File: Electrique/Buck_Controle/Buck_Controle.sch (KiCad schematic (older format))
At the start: 0 parts

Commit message: footprint - pcb build
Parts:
- added Cboot1: 10nF, Capacitor_SMD:C_0805_2012Metric, symbol Device:C_Small
- added Cin1, Cin2, Cin3: 10uF, Capacitor_SMD:C_0805_2012Metric, symbol Device:C_Small
- added Cout1: 330uF, Buck_Controle:CAP_TANT_2917, symbol Device:CP1_Small
- added D1: SBRD10200TR, Diode_SMD:D_SMC, symbol Device:D
- added L1: 15uH, Inductor_SMD:L_Bourns_SRR1210A, symbol Device:L
- added Rfbb1: 3.24k, Resistor_SMD:R_0805_2012Metric, symbol Device:R
- added Rfbt1: 10k, Resistor_SMD:R_0805_2012Metric, symbol Device:R
- added U1: TPS5450DDA, Package_SO:TI_SO-PowerPAD-8_ThermalVias, symbol Custom_parts:TPS5450DDA
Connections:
- new net: Cboot1.1, D1.1 (K), L1.2, U1.1 (BOOT)
- new net: Rfbb1.1, Rfbt1.2, U1.4 (VSENSE)
- new net: Cboot1.2, U1.8 (PH)
- new net +BATT: Cin1.1, Cin2.1, Cin3.1, U1.7 (VIN)
- new net GND: Cin1.2, Cin2.2, Cin3.2, Cout1.2, D1.2 (A), Rfbb1.2, U1.6 (GND), U1.9 (PW_PAD)
- new net Vout: Cout1.1, L1.1, Rfbt1.1
- no-connect marks 0 -> 1

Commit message: Continuation PCB controle
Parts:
- added J?: Conn_01x02_Female, symbol Connector:Conn_01x02_Female
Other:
- moved on the sheet: Cboot1, Cin1, Cin2, Cin3, Cout1, D1, L1, Rfbb1, Rfbt1, U1

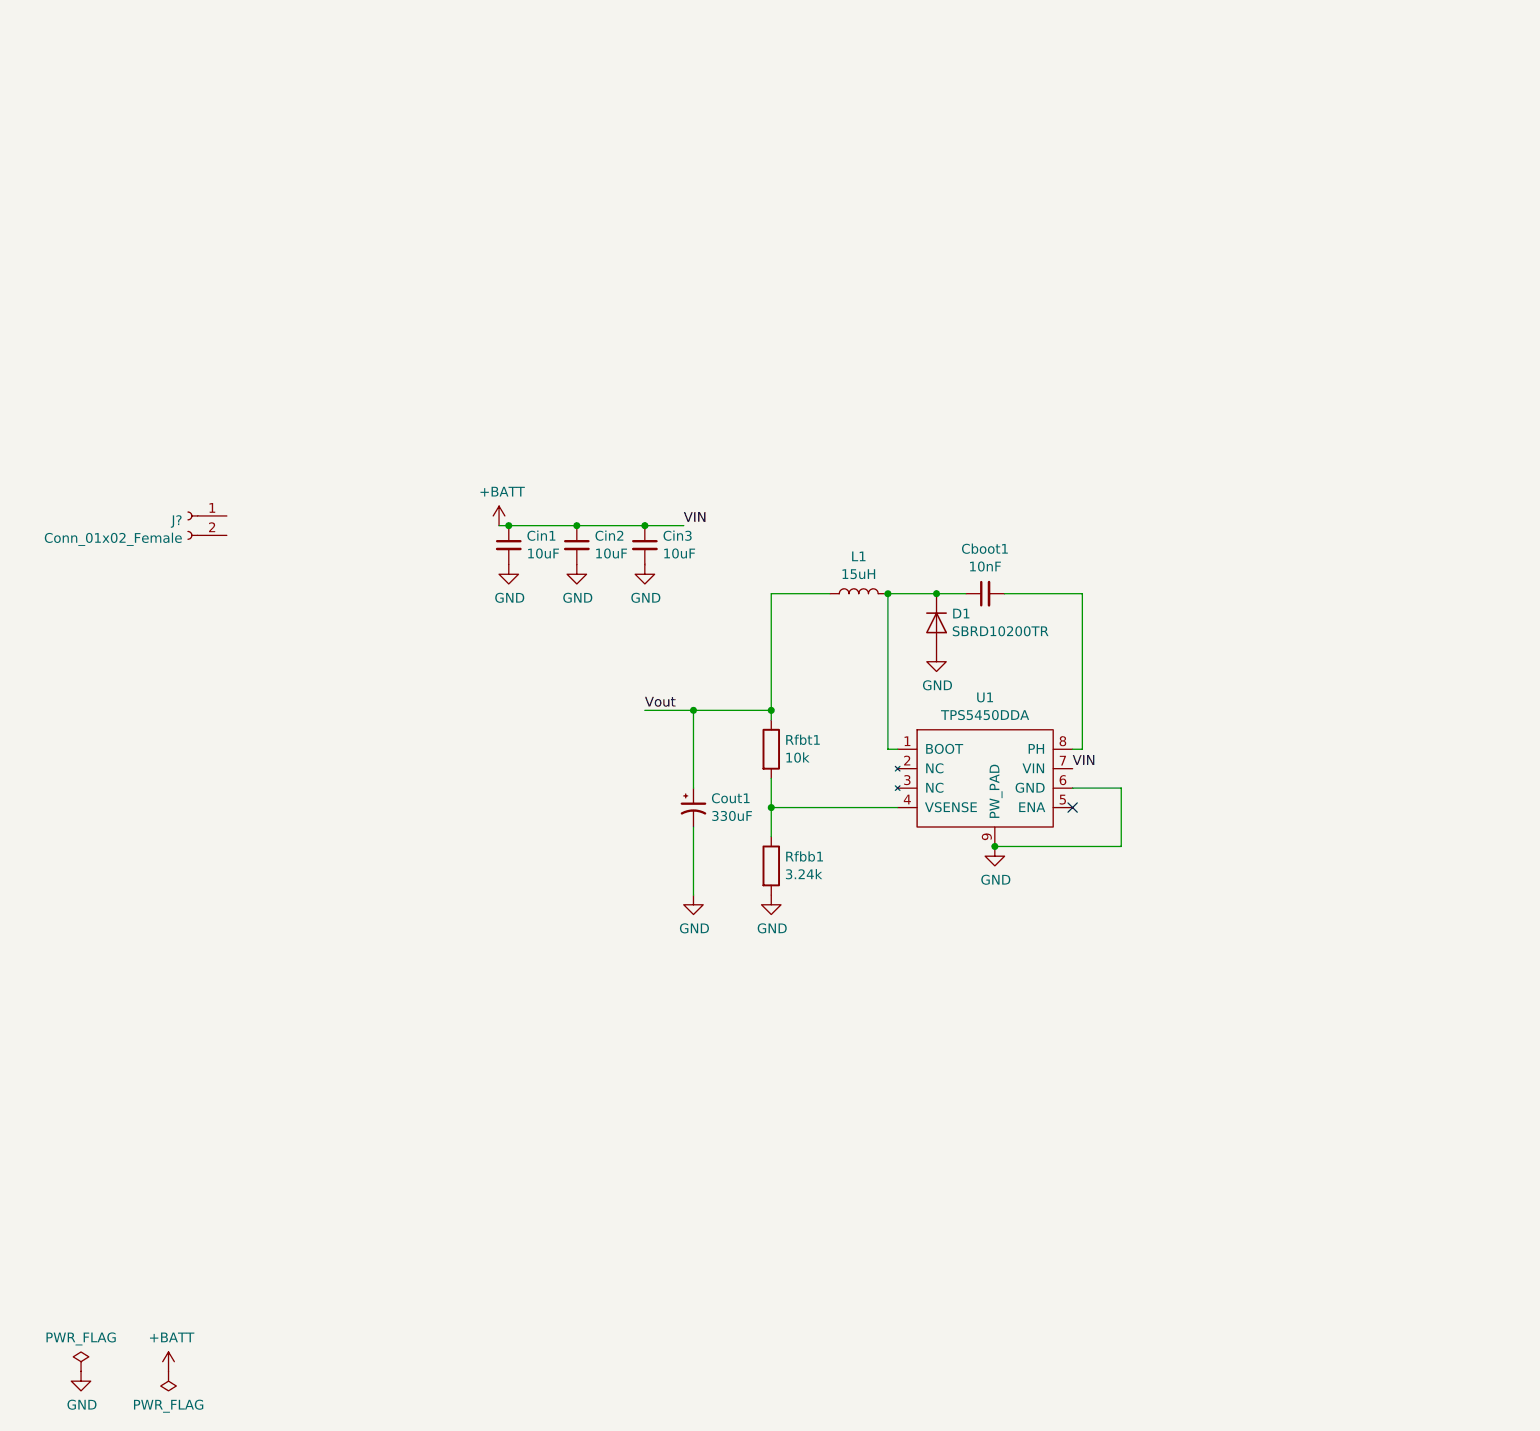
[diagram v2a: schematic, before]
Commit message: Ajout pieces manquantes Boost
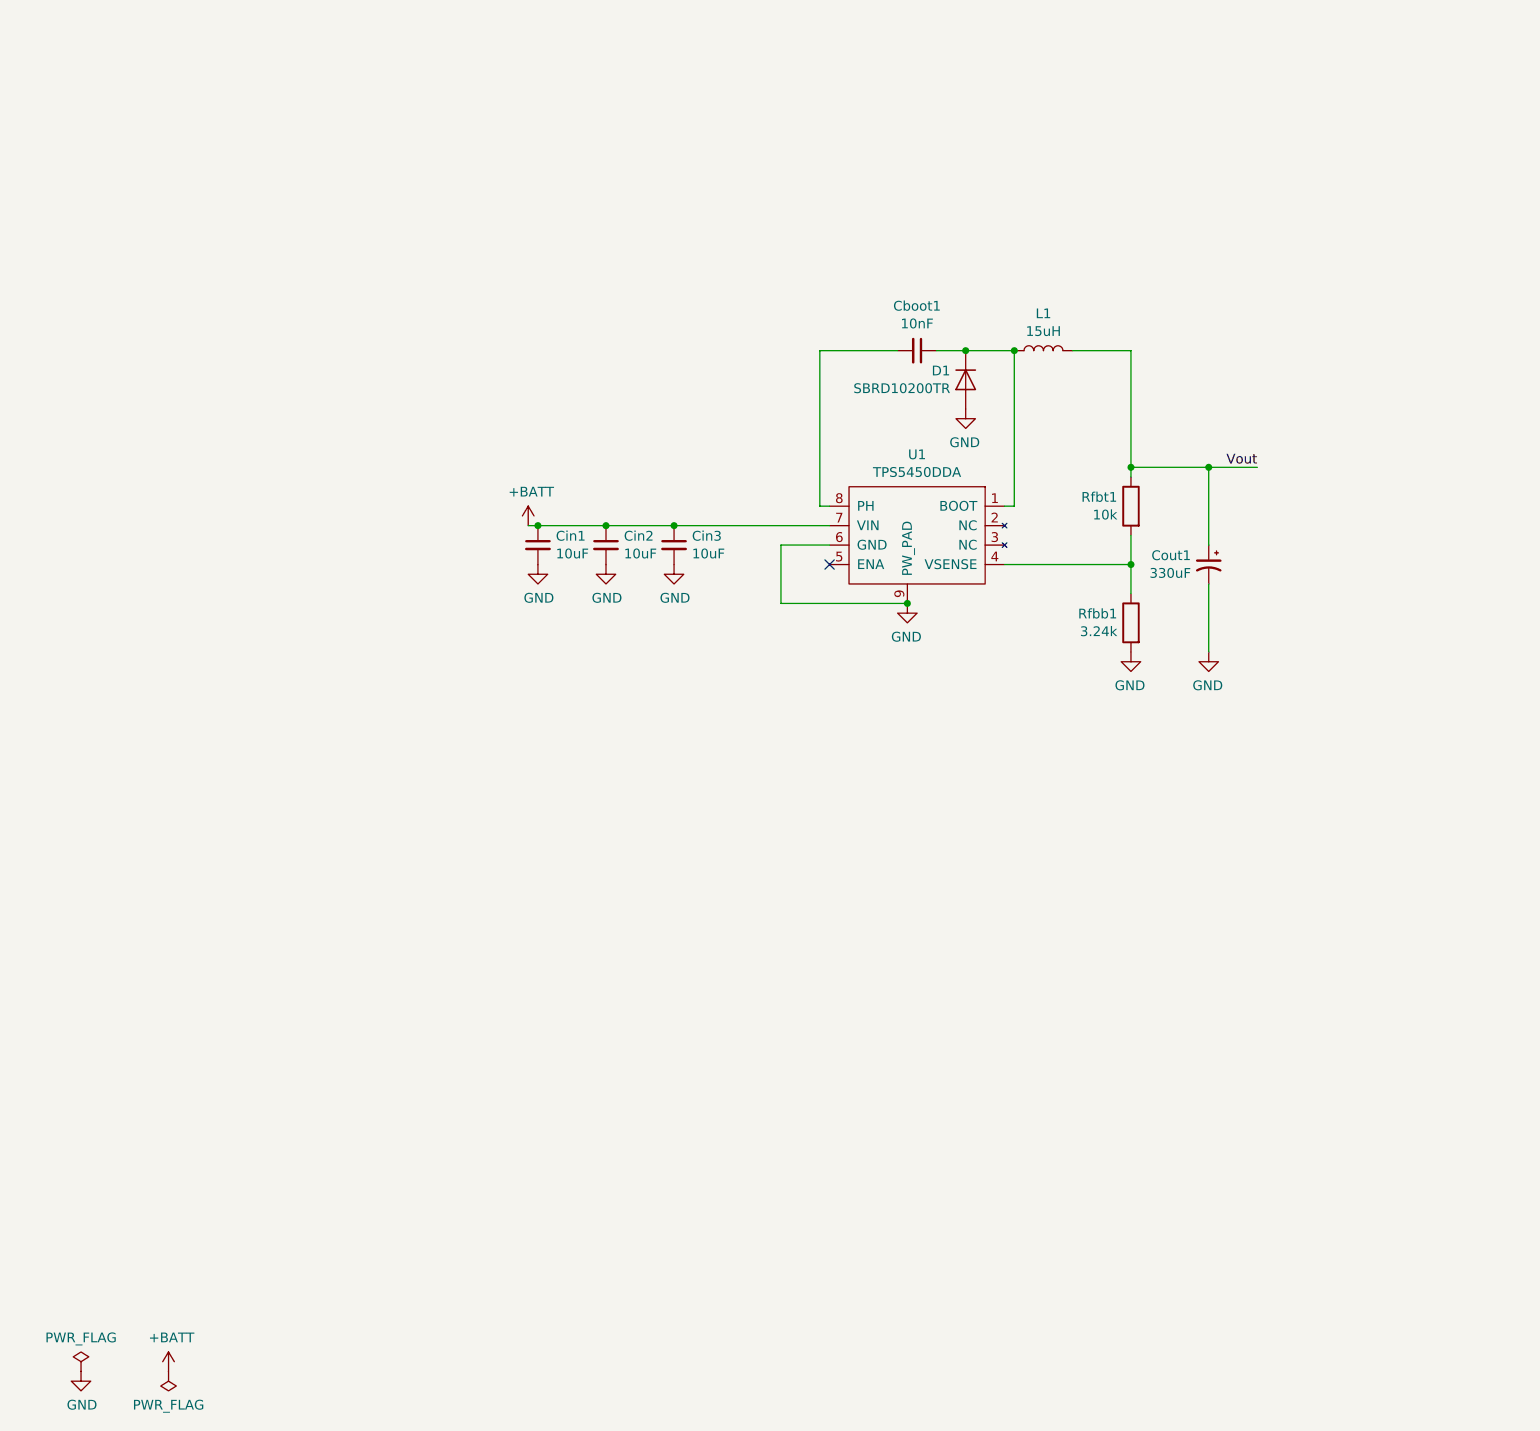
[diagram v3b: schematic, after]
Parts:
- removed J?: Conn_01x02_Female, symbol Connector:Conn_01x02_Female
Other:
- moved on the sheet: Cboot1, Cin1, Cin2, Cin3, Cout1, D1, L1, Rfbb1, Rfbt1, U1

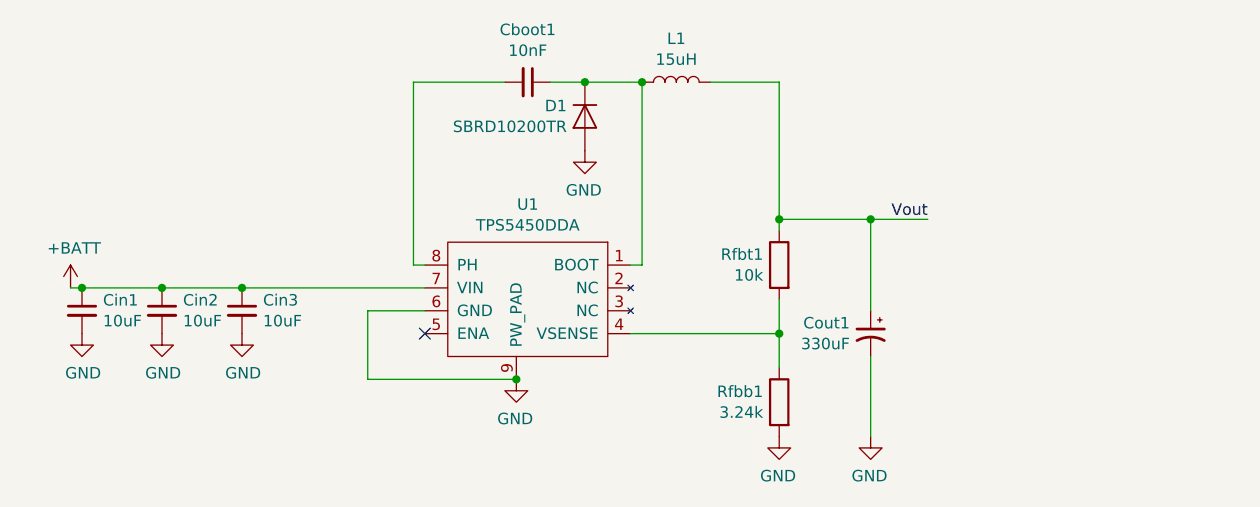
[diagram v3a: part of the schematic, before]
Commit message: Ajout du bus in/out
Ajout du bus pour in/out + routage sur la couche du dessous + via pour transférer ces signaux sur les 2 couches
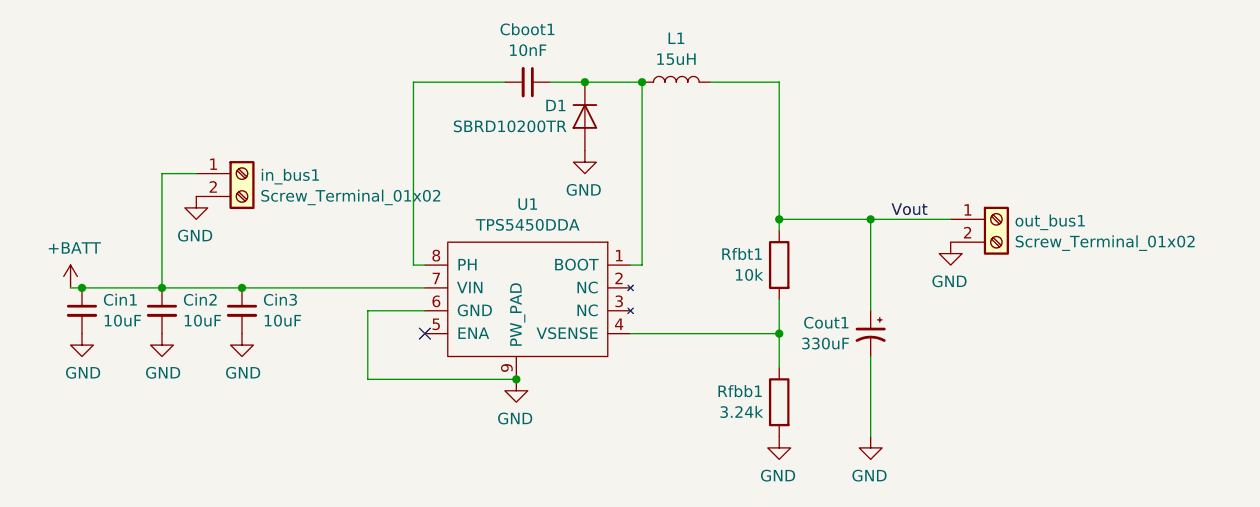
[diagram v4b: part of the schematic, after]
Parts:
- added in_bus1, out_bus1: Screw_Terminal_01x02, TerminalBlock:TerminalBlock_bornier-2_P5.08mm, symbol Connector:Screw_Terminal_01x02
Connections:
- net +BATT: now also in_bus1.1 (Pin_1)
- net GND: now also in_bus1.2 (Pin_2), out_bus1.2 (Pin_2)
- net Vout: now also out_bus1.1 (Pin_1)
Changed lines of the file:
@@
 Wire Wire Line
 	7100 3600 7100 3950
-Wire Wire Line
-	7100 3000 7350 3000
 Connection ~ 7100 3000
 Text Label 7350 3000 2    50   ~ 0
@@
 Wire Wire Line
 	4350 3300 5150 3300
+$Comp
+L Connector:Screw_Terminal_01x02 in_bus1
+U 1 1 5FBC6AC6
+P 4350 2800
+F 0 "in_bus1" H 4430 2792 50  0000 L CNN
+F 1 "Screw_Terminal_01x02" H 4430 2701 50  0000 L CNN
+F 2 "TerminalBlock:TerminalBlock_bornier-2_P5.08mm" H 4350 2800 50  0001 C CNN
+F 3 "~" H 4350 2800 50  0001 C CNN
+	1    4350 2800
+	1    0    0    -1
+$EndComp
+$Comp
+L Connector:Screw_Terminal_01x02 out_bus1
+U 1 1 5FBC7ECB
+P 7650 3000
+F 0 "out_bus1" H 7730 2992 50  0000 L CNN
+F 1 "Screw_Terminal_01x02" H 7730 2901 50  0000 L CNN
+F 2 "TerminalBlock:TerminalBlock_bornier-2_P5.08mm" H 7650 3000 50  0001 C CNN
+F 3 "~" H 7650 3000 50  0001 C CNN
+	1    7650 3000
+	1    0    0    -1
+$EndComp
+$Comp
+L power:GND #PWR0111
+U 1 1 5FBC9301
+P 7450 3100
+F 0 "#PWR0111" H 7450 2850 50  0001 C CNN
+F 1 "GND" H 7455 2927 50  0000 C CNN
+F 2 "" H 7450 3100 50  0001 C CNN
+F 3 "" H 7450 3100 50  0001 C CNN
+	1    7450 3100
+	-1   0    0    -1
+$EndComp
+$Comp
+L power:GND #PWR0112
+U 1 1 5FBCA470
+P 4150 2900
+F 0 "#PWR0112" H 4150 2650 50  0001 C CNN
+F 1 "GND" H 4155 2727 50  0000 C CNN
+F 2 "" H 4150 2900 50  0001 C CNN
+F 3 "" H 4150 2900 50  0001 C CNN
+	1    4150 2900
+	-1   0    0    -1
+$EndComp
+Wire Wire Line
+	4150 2800 4000 2800
+Wire Wire Line
+	4000 2800 4000 3300
+Wire Wire Line
+	7100 3000 7450 3000
 $EndSCHEMATC

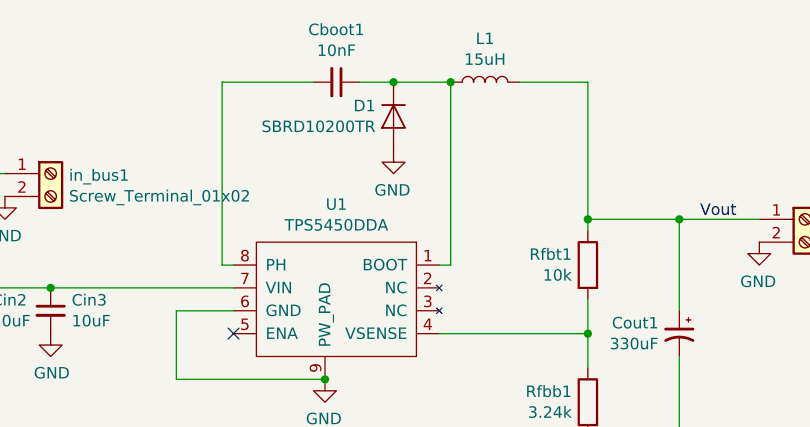
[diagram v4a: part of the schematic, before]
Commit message: Changement du branchement de Cboot + DRC pcb controle
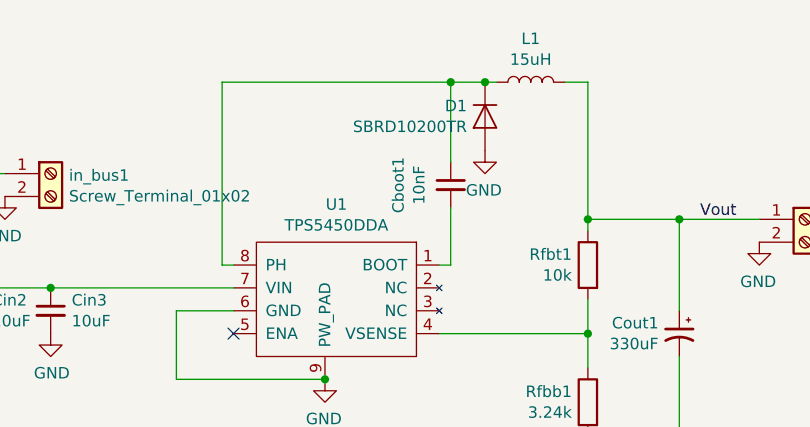
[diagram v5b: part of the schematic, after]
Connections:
- net at Cboot1.1, D1.1 (K), L1.2: now also U1.8 (PH); no longer U1.1 (BOOT)
- net at Cboot1.2: now also U1.1 (BOOT); no longer U1.8 (PH)
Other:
- moved on the sheet: Cboot1, D1, L1
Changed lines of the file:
@@
 L Device:C_Small Cboot1
 U 1 1 5E446D6F
-P 5600 2400
-F 0 "Cboot1" V 5829 2400 50  0000 C CNN
-F 1 "10nF" V 5738 2400 50  0000 C CNN
-F 2 "Capacitor_SMD:C_0805_2012Metric" H 5600 2400 50  0001 C CNN
-F 3 "~" H 5600 2400 50  0001 C CNN
-	1    5600 2400
-	0    1    -1   0
+P 6100 2850
+F 0 "Cboot1" V 6329 2850 50  0000 C CNN
+F 1 "10nF" V 6238 2850 50  0000 C CNN
+F 2 "Capacitor_SMD:C_0805_2012Metric" H 6100 2850 50  0001 C CNN
+F 3 "~" H 6100 2850 50  0001 C CNN
+	1    6100 2850
+	-1   0    0    -1
 $EndComp
 Wire Wire Line
 	6100 3200 6050 3200
 Wire Wire Line
-	5500 2400 5100 2400
-Wire Wire Line
 	5100 3200 5150 3200
 Wire Wire Line
-	5700 2400 5850 2400
-Wire Wire Line
 	5100 2400 5100 3200
 Wire Wire Line
-	6100 2400 6100 3200
+	6100 2400 6100 2750
 $Comp
 L Device:D D1
 U 1 1 5E44E25D
-P 5850 2550
-F 0 "D1" V 5804 2629 50  0000 L CNN
-F 1 "SBRD10200TR" V 5895 2629 50  0000 L CNN
-F 2 "Diode_SMD:D_SMC" H 5850 2550 50  0001 C CNN
-F 3 "~" H 5850 2550 50  0001 C CNN
-	1    5850 2550
+P 6250 2550
+F 0 "D1" V 6204 2629 50  0000 L CNN
+F 1 "SBRD10200TR" V 6295 2629 50  0000 L CNN
+F 2 "Diode_SMD:D_SMC" H 6250 2550 50  0001 C CNN
+F 3 "~" H 6250 2550 50  0001 C CNN
+	1    6250 2550
 	0    -1   1    0
 $EndComp
-Connection ~ 5850 2400
-Wire Wire Line
-	5850 2400 6100 2400
 $Comp
 L power:GND #PWR0104
 U 1 1 5E44E60C
-P 5850 2700
-F 0 "#PWR0104" H 5850 2450 50  0001 C CNN
-F 1 "GND" H 5855 2527 50  0000 C CNN
-F 2 "" H 5850 2700 50  0001 C CNN
-F 3 "" H 5850 2700 50  0001 C CNN
-	1    5850 2700
+P 6250 2700
+F 0 "#PWR0104" H 6250 2450 50  0001 C CNN
+F 1 "GND" H 6255 2527 50  0000 C CNN
+F 2 "" H 6250 2700 50  0001 C CNN
+F 3 "" H 6250 2700 50  0001 C CNN
+	1    6250 2700
 	-1   0    0    -1
 $EndComp
@@
 L Device:L L1
 U 1 1 5E44F76F
-P 6250 2400
-F 0 "L1" V 6440 2400 50  0000 C CNN
-F 1 "15uH" V 6349 2400 50  0000 C CNN
-F 2 "Inductor_SMD:L_Bourns_SRR1210A" H 6250 2400 50  0001 C CNN
-F 3 "~" H 6250 2400 50  0001 C CNN
-	1    6250 2400
+P 6450 2400
+F 0 "L1" V 6640 2400 50  0000 C CNN
+F 1 "15uH" V 6549 2400 50  0000 C CNN
+F 2 "Inductor_SMD:L_Bourns_SRR1210A" H 6450 2400 50  0001 C CNN
+F 3 "~" H 6450 2400 50  0001 C CNN
+	1    6450 2400
 	0    1    -1   0
 $EndComp
-Connection ~ 6100 2400
 $Comp
 L Device:R Rfbt1
@@
 Wire Wire Line
 	6700 3050 6700 3000
-Wire Wire Line
-	6700 2400 6400 2400
 $Comp
 L power:GND #PWR0105
@@
 Wire Wire Line
 	7100 3000 7450 3000
+Wire Wire Line
+	6100 2950 6100 3200
+Wire Wire Line
+	6700 2400 6600 2400
+Wire Wire Line
+	6300 2400 6250 2400
+Connection ~ 6100 2400
+Connection ~ 6250 2400
+Wire Wire Line
+	6250 2400 6100 2400
+Wire Wire Line
+	5100 2400 6100 2400
 $EndSCHEMATC
